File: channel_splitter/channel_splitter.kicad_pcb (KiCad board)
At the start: 2 copper layers, 213 x 80 mm, 70 parts, among them J1 USB_B, J2 MIDI IN, J3 ICSP, J4 Conn_01x05, J5 MIDI OUT 1, J6 MIDI OUT 2, J7 MIDI OUT 3, J8 MIDI OUT 4, J9 MIDI THRU, Q1 MMBT3906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

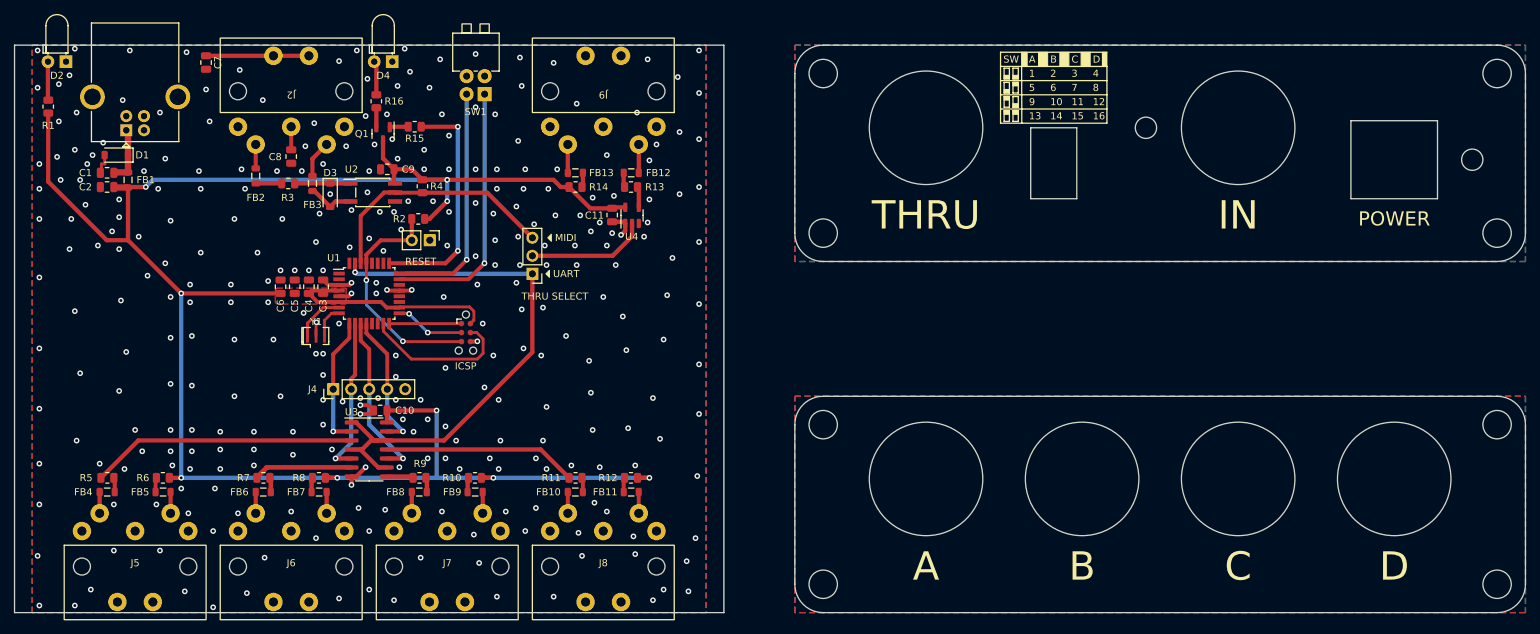
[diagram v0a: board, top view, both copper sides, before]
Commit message: Add version info to silkscreen. update gerbers
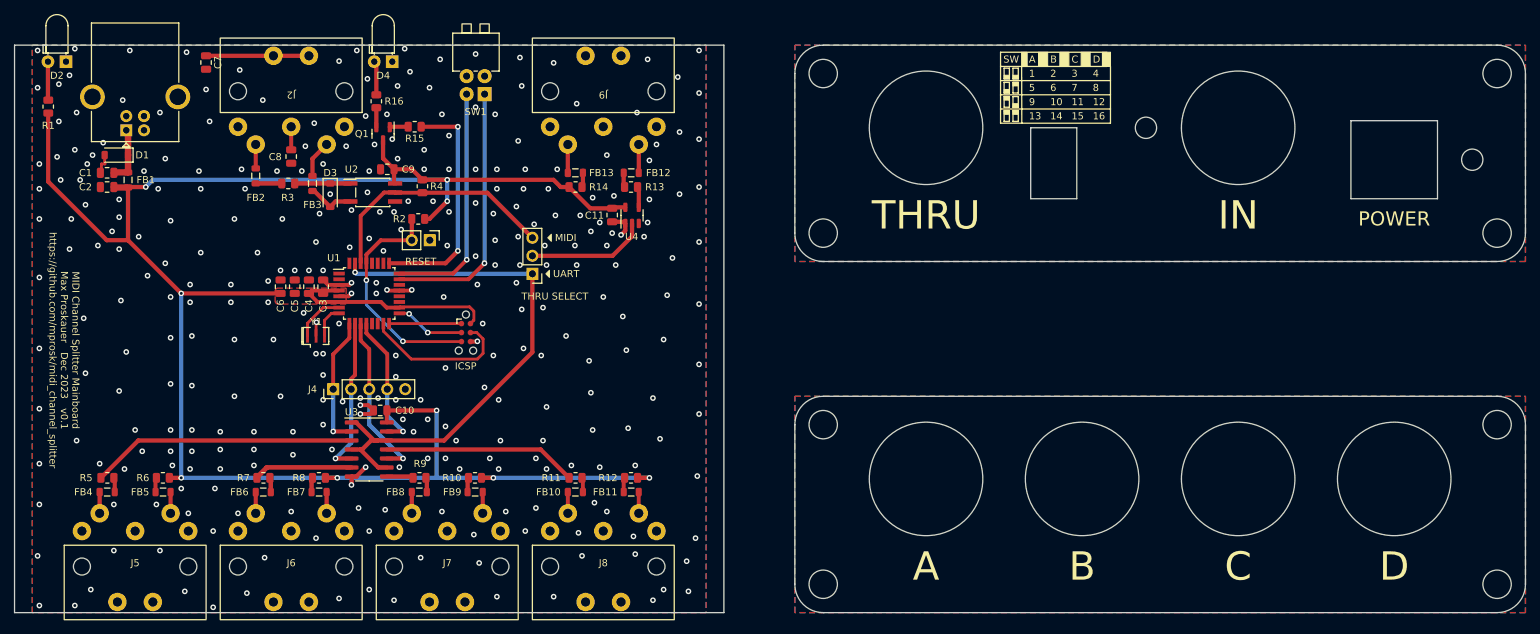
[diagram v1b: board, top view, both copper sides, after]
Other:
- board text added: "MIDI Channel Splitter Front Panel Max Proskauer Dec 2023 v0.1 https://github.com/mprosk/midi_channel_splitter"
- board text added: "MIDI Channel Splitter Mainboard Max Proskauer Dec 2023 v0.1 https://github.com/mprosk/midi_channel_splitter"
- board text added: "MIDI Channel Splitter Rear Panel Max Proskauer Dec 2023 v0.1 https://github.com/mprosk/midi_channel_splitter"
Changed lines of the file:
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@@
     )
   )
-  (gr_line (start 204 79) (end 189 79)
+  (gr_line (start 204.5 79) (end 189 79)
     (stroke (width 0.15) (type solid)) (layer "F.SilkS"))
   (gr_rect (start 200.3623 71) (end 201.6377 73)
@@
   (gr_rect (start 190.75 75.25) (end 191.5 76.75)
     (stroke (width 0.15) (type solid)) (fill none) (layer "F.SilkS"))
-  (gr_rect (start 203.3623 71) (end 204 73)
+  (gr_rect (start 203.3623 71) (end 204.5 73)
     (stroke (width 0.15) (type solid)) (fill solid) (layer "F.SilkS"))
   (gr_rect (start 190.75 77.25) (end 191.5 78.75)
@@
   (gr_rect (start 190.75 79.25) (end 191.5 80.75)
     (stroke (width 0.15) (type solid)) (fill none) (layer "F.SilkS"))
-  (gr_line (start 189 81) (end 204 81)
+  (gr_line (start 189 81) (end 204.5 81)
     (stroke (width 0.15) (type default)) (layer "F.SilkS"))
   (gr_rect (start 190.75 74.25) (end 191.5 74.75)
@@
   (gr_rect (start 189.5 77.25) (end 190.25 78.75)
     (stroke (width 0.15) (type solid)) (fill none) (layer "F.SilkS"))
-  (gr_line (start 204 81) (end 204 73)
+  (gr_line (start 204.5 81) (end 204.5 73)
     (stroke (width 0.15) (type solid)) (layer "F.SilkS"))
   (gr_rect (start 190.75 78.25) (end 191.5 78.75)
@@
   (gr_rect (start 189.5 79.25) (end 190.25 80.75)
     (stroke (width 0.15) (type solid)) (fill none) (layer "F.SilkS"))
-  (gr_line (start 189 77) (end 204 77)
+  (gr_line (start 189 77) (end 204.5 77)
     (stroke (width 0.15) (type default)) (layer "F.SilkS"))
   (gr_rect (start 189.5 77.25) (end 190.25 77.75)
@@
   (gr_rect (start 190.75 75.25) (end 191.5 75.75)
     (stroke (width 0.15) (type solid)) (fill solid) (layer "F.SilkS"))
-  (gr_line (start 189 75) (end 204 75)
+  (gr_line (start 189 75) (end 204.5 75)
     (stroke (width 0.15) (type default)) (layer "F.SilkS"))
   (gr_line (start 50 68.6) (end 150 68.6)
@@
     (effects (font (size 1 1) (thickness 0.15)) (justify mirror))
   )
+  (gr_text "MIDI Channel Splitter Rear Panel\nMax Proskauer   Dec 2023   v0.1\nhttps://github.com/mprosk/midi_channel_splitter" (at 211.5 95) (layer "B.SilkS")
+    (effects (font (size 1 1) (thickness 0.15)) (justify mirror))
+  )
   (gr_text "JLCJLCJLCJLC" (at 54.5 140 90) (layer "B.SilkS")
     (effects (font (size 1 1) (thickness 0.15)) (justify mirror))
   )
+  (gr_text "MIDI Channel Splitter Front Panel\nMax Proskauer   Dec 2023   v0.1\nhttps://github.com/mprosk/midi_channel_splitter" (at 211.5 144.5) (layer "B.SilkS")
+    (effects (font (size 1 1) (thickness 0.15)) (justify mirror))
+  )
   (gr_text "JLCJLCJLCJLC" (at 211.5 99.5) (layer "B.SilkS")
     (effects (font (size 1 1) (thickness 0.15)) (justify mirror))
@@
   )
   (gr_text "SW" (at 190.5 72) (layer "F.SilkS" knockout)
+    (effects (font (size 1 1) (thickness 0.15)))
+  )
+  (gr_text "MIDI Channel Splitter Mainboard\nMax Proskauer   Dec 2023   v0.1\nhttps://github.com/mprosk/midi_channel_splitter" (at 57 113 270) (layer "F.SilkS")
     (effects (font (size 1 1) (thickness 0.15)))
   )
@@
   (via (at 82 87.5) (size 0.8) (drill 0.4) (layers "F.Cu" "B.Cu") (free) (net 1))
   (via (at 117.75 97.5) (size 0.8) (drill 0.4) (layers "F.Cu" "B.Cu") (free) (net 1))
-  (via (at 58.5 107.5) (size 0.8) (drill 0.4) (layers "F.Cu" "B.Cu") (free) (net 1))
+  (via (at 59.75 108.5) (size 0.8) (drill 0.4) (layers "F.Cu" "B.Cu") (free) (net 1))
   (via (at 140 119.75) (size 0.8) (drill 0.4) (layers "F.Cu" "B.Cu") (free) (net 1))
   (via (at 119.25 135.75) (size 0.8) (drill 0.4) (layers "F.Cu" "B.Cu") (free) (net 1))
@@
   (via (at 65.5 129.75) (size 0.8) (drill 0.4) (layers "F.Cu" "B.Cu") (free) (net 1))
   (via (at 83.75 124.5) (size 0.8) (drill 0.4) (layers "F.Cu" "B.Cu") (free) (net 1))
-  (via (at 59.25 116.25) (size 0.8) (drill 0.4) (layers "F.Cu" "B.Cu") (free) (net 1))
+  (via (at 60 116.25) (size 0.8) (drill 0.4) (layers "F.Cu" "B.Cu") (free) (net 1))
   (via (at 61 85.5) (size 0.8) (drill 0.4) (layers "F.Cu" "B.Cu") (free) (net 1))
   (via (at 95.75 109.25) (size 0.8) (drill 0.4) (layers "F.Cu" "B.Cu") (free) (net 1))
